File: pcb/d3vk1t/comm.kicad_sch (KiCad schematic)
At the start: 14 parts, among them IC5 TJA1042T/3/1J, IC6 MAX3485CSA+T, J4 Conn_01x03, J5 Conn_01x03

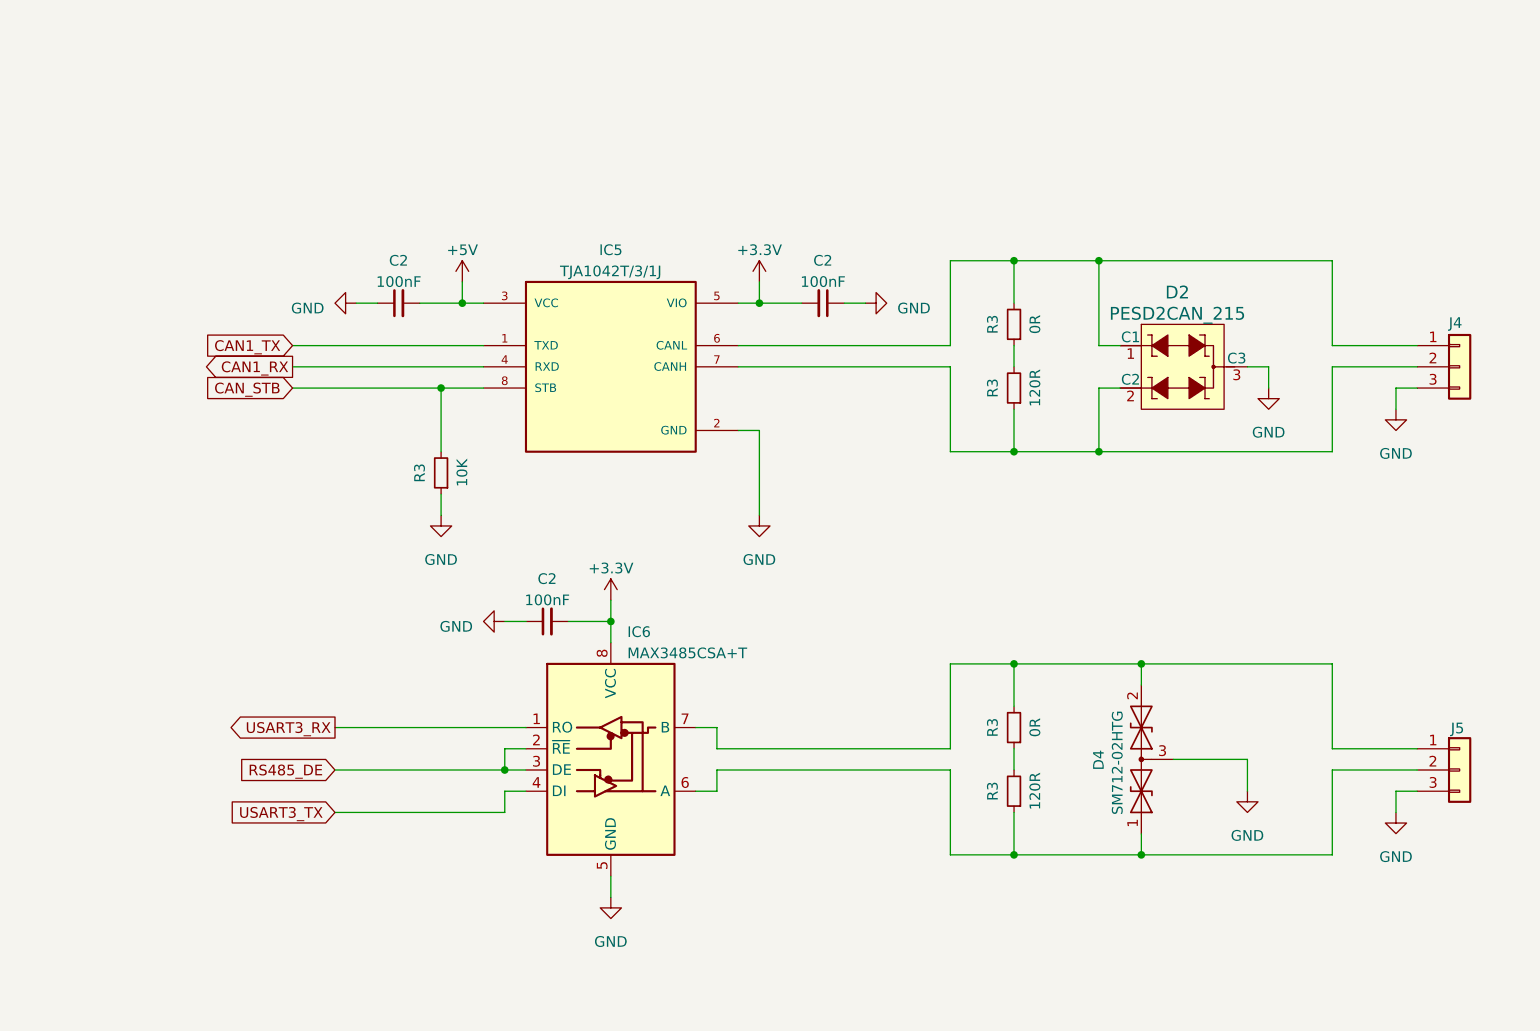
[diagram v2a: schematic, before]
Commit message: pcb: update layout
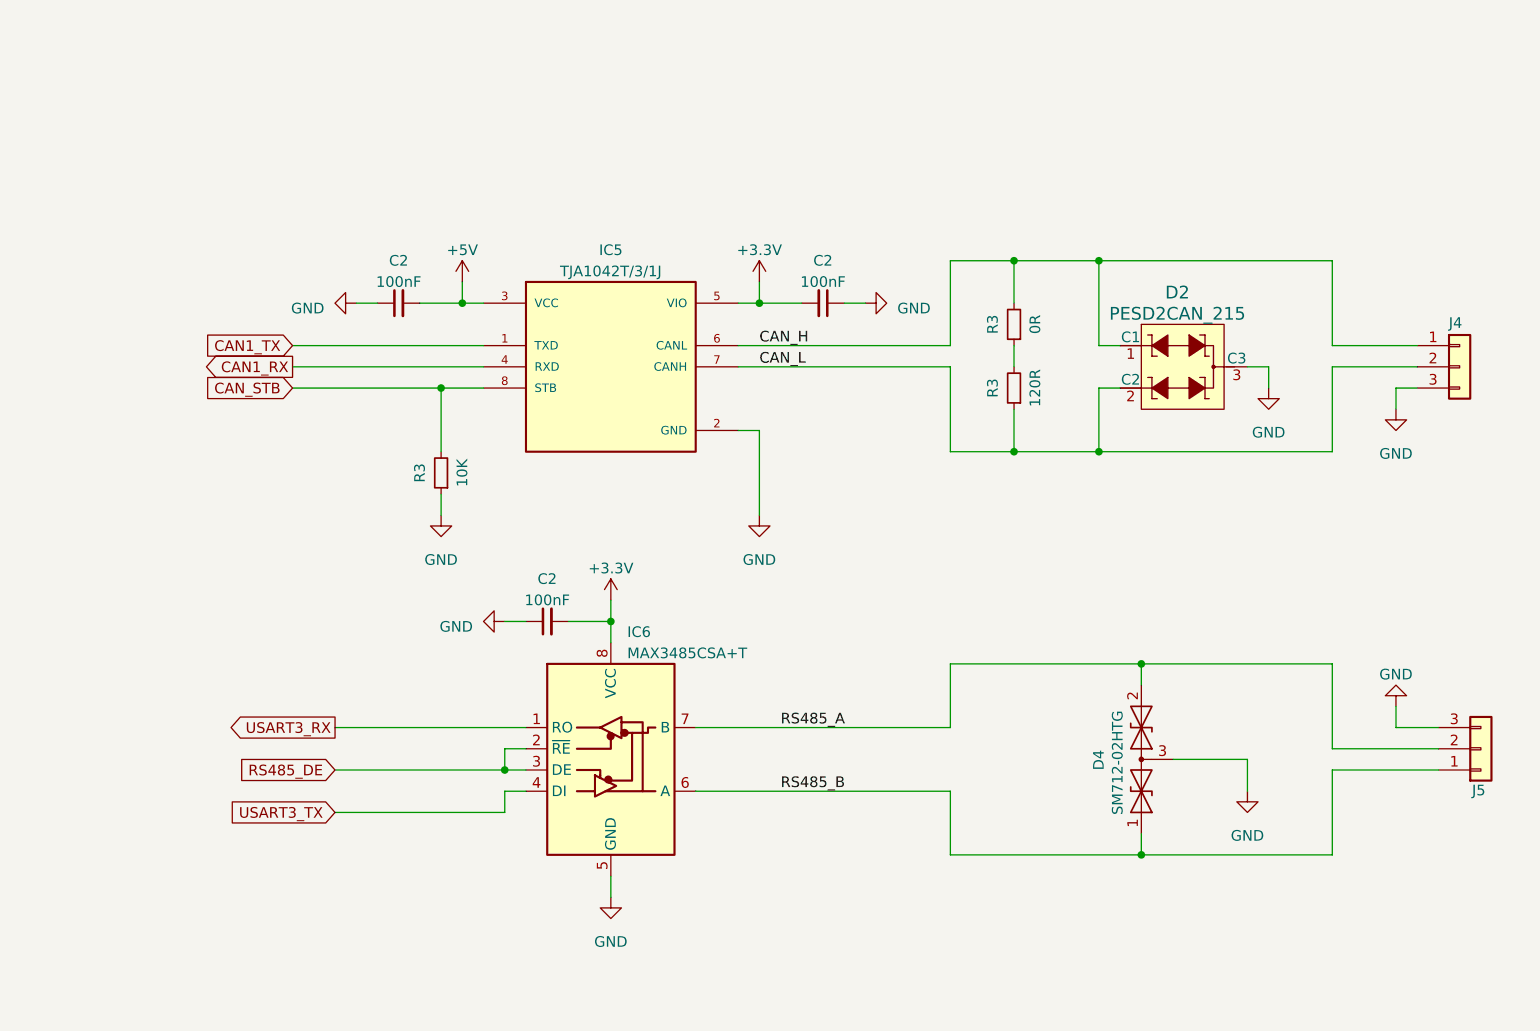
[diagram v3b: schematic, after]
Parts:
- removed R3: 120R, Resistor_SMD:R_0402_1005Metric, symbol Device:R_Small
- removed R3: 0R, Resistor_SMD:R_0402_1005Metric, symbol Device:R_Small
- D2: footprint digikey-footprints:SOT-23-3 -> bruno-libs:SOT-23B
- D4: footprint Package_TO_SOT_SMD:SOT-23 -> bruno-libs:SOT-23B
- IC6: footprint Package_SO:SOIC-8W_5.3x5.3mm_P1.27mm -> db:SOIC127P600X175-8N
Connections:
- net RS485_A: now reaches D4.2 (A2), IC6.7 (B)
- net RS485_A: now also J5.2 (Pin_2); no longer J5.1 (Pin_1)
- net RS485_B: now reaches D4.1 (A1), IC6.6 (A)
- net RS485_B: now also J5.1 (Pin_1); no longer J5.2 (Pin_2)
- net CAN_L: now reaches D2.2 (C2), IC5.7 (CANH), J4.2 (Pin_2), R3.1
- net CAN_H: now reaches D2.1 (C1), IC5.6 (CANL), J4.1 (Pin_1), R3.2
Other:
- moved on the sheet: J5
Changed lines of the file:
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@@
   (junction (at 187.96 86.36) (diameter 0) (color 0 0 0 0)
   )
-  (junction (at 177.8 134.62) (diameter 0) (color 0 0 0 0)
-  )
   (junction (at 187.96 63.5) (diameter 0) (color 0 0 0 0)
   )
   (junction (at 129.54 106.68) (diameter 0) (color 0 0 0 0)
   )
-  (junction (at 177.8 111.76) (diameter 0) (color 0 0 0 0)
-  )
   (junction (at 109.22 78.74) (diameter 0) (color 0 0 0 0)
   )
@@
     (stroke (width 0) (type default))
   )
-  (wire (pts (xy 215.9 121.92) (xy 226.06 121.92))
-    (stroke (width 0) (type default))
-  )
   (wire (pts (xy 109.22 86.36) (xy 109.22 78.74))
     (stroke (width 0) (type default))
@@
     (stroke (width 0) (type default))
   )
-  (wire (pts (xy 177.8 134.62) (xy 193.04 134.62))
-    (stroke (width 0) (type default))
-  )
   (wire (pts (xy 109.22 91.44) (xy 109.22 93.98))
     (stroke (width 0) (type default))
@@
     (stroke (width 0) (type default))
   )
-  (wire (pts (xy 170.18 111.76) (xy 177.8 111.76))
-    (stroke (width 0) (type default))
-  )
-  (wire (pts (xy 223.52 129.54) (xy 223.52 127))
+  (wire (pts (xy 223.52 119.38) (xy 223.52 116.84))
     (stroke (width 0) (type default))
   )
@@
     (stroke (width 0) (type default))
   )
-  (wire (pts (xy 177.8 121.92) (xy 177.8 124.46))
-    (stroke (width 0) (type default))
-  )
   (wire (pts (xy 124.46 106.68) (xy 129.54 106.68))
     (stroke (width 0) (type default))
@@
     (stroke (width 0) (type default))
   )
-  (wire (pts (xy 215.9 124.46) (xy 226.06 124.46))
-    (stroke (width 0) (type default))
-  )
-  (wire (pts (xy 170.18 124.46) (xy 170.18 134.62))
+  (wire (pts (xy 223.52 119.38) (xy 228.6 119.38))
+    (stroke (width 0) (type default))
+  )
+  (wire (pts (xy 170.18 127) (xy 170.18 134.62))
     (stroke (width 0) (type default))
   )
@@
     (stroke (width 0) (type default))
   )
-  (wire (pts (xy 177.8 111.76) (xy 193.04 111.76))
+  (wire (pts (xy 170.18 111.76) (xy 193.04 111.76))
     (stroke (width 0) (type default))
   )
@@
     (stroke (width 0) (type default))
   )
+  (wire (pts (xy 215.9 124.46) (xy 228.6 124.46))
+    (stroke (width 0) (type default))
+  )
   (wire (pts (xy 91.44 78.74) (xy 109.22 78.74))
     (stroke (width 0) (type default))
@@
     (stroke (width 0) (type default))
   )
-  (wire (pts (xy 139.7 127) (xy 142.24 127))
-    (stroke (width 0) (type default))
-  )
-  (wire (pts (xy 177.8 111.76) (xy 177.8 116.84))
+  (wire (pts (xy 139.7 127) (xy 170.18 127))
     (stroke (width 0) (type default))
   )
@@
     (stroke (width 0) (type default))
   )
-  (wire (pts (xy 170.18 134.62) (xy 177.8 134.62))
-    (stroke (width 0) (type default))
-  )
-  (wire (pts (xy 139.7 119.38) (xy 142.24 119.38))
-    (stroke (width 0) (type default))
-  )
-  (wire (pts (xy 142.24 121.92) (xy 142.24 119.38))
+  (wire (pts (xy 170.18 134.62) (xy 193.04 134.62))
     (stroke (width 0) (type default))
   )
@@
     (stroke (width 0) (type default))
   )
-  (wire (pts (xy 142.24 124.46) (xy 170.18 124.46))
-    (stroke (width 0) (type default))
-  )
   (wire (pts (xy 215.9 86.36) (xy 215.9 76.2))
     (stroke (width 0) (type default))
   )
-  (wire (pts (xy 142.24 121.92) (xy 170.18 121.92))
-    (stroke (width 0) (type default))
-  )
-  (wire (pts (xy 223.52 127) (xy 226.06 127))
+  (wire (pts (xy 139.7 119.38) (xy 170.18 119.38))
     (stroke (width 0) (type default))
   )
@@
     (stroke (width 0) (type default))
   )
-  (wire (pts (xy 170.18 121.92) (xy 170.18 111.76))
-    (stroke (width 0) (type default))
-  )
-  (wire (pts (xy 142.24 127) (xy 142.24 124.46))
+  (wire (pts (xy 170.18 119.38) (xy 170.18 111.76))
     (stroke (width 0) (type default))
   )
@@
     (stroke (width 0) (type default))
   )
+  (wire (pts (xy 215.9 121.92) (xy 228.6 121.92))
+    (stroke (width 0) (type default))
+  )
   (wire (pts (xy 116.84 124.46) (xy 119.38 124.46))
     (stroke (width 0) (type default))
@@
     (stroke (width 0) (type default))
   )
-  (wire (pts (xy 177.8 129.54) (xy 177.8 134.62))
-    (stroke (width 0) (type default))
+  (label "CAN_H" (at 147.32 73.66 0) (fields_autoplaced)
+    (effects (font (size 1.27 1.27)) (justify left bottom))
+  )
+  (label "RS485_A" (at 149.86 119.38 0) (fields_autoplaced)
+    (effects (font (size 1.27 1.27)) (justify left bottom))
+  )
+  (label "RS485_B" (at 149.86 127 0) (fields_autoplaced)
+    (effects (font (size 1.27 1.27)) (justify left bottom))
+  )
+  (label "CAN_L" (at 147.32 76.2 0) (fields_autoplaced)
+    (effects (font (size 1.27 1.27)) (justify left bottom))
   )
   (global_label "CAN1_TX" (shape input) (at 91.44 73.66 180) (fields_autoplaced)
@@
     )
   )
-  (symbol (lib_id "Connector_Generic:Conn_01x03") (at 231.14 124.46 0) (unit 1)
+  (symbol (lib_id "Connector_Generic:Conn_01x03") (at 233.68 121.92 0) (mirror x) (unit 1)
     (in_bom yes) (on_board yes) (dnp no)
-    (property "Reference" "J5" (at 230.0818 119.4761 0)
+    (property "Reference" "J5" (at 232.6218 126.9039 0)
       (effects (font (size 1.27 1.27)) (justify left))
     )
-    (property "Value" "Conn_01x03" (at 233.68 126.365 0)
+    (property "Value" "Conn_01x03" (at 236.22 120.015 0)
       (effects (font (size 1.27 1.27)) (justify left) hide)
     )
-    (property "Footprint" "Connector_JST:JST_XH_B3B-XH-A_1x03_P2.50mm_Vertical" (at 231.14 124.46 0)
-      (effects (font (size 1.27 1.27)) hide)
-    )
-    (property "Datasheet" "~" (at 231.14 124.46 0)
+    (property "Footprint" "Connector_JST:JST_XH_B3B-XH-A_1x03_P2.50mm_Vertical" (at 233.68 121.92 0)
+      (effects (font (size 1.27 1.27)) hide)
+    )
+    (property "Datasheet" "~" (at 233.68 121.92 0)
       (effects (font (size 1.27 1.27)) hide)
     )
@@
     )
   )
-  (symbol (lib_id "Device:R_Small") (at 177.8 127 180) (unit 1)
-    (in_bom yes) (on_board yes) (dnp no)
-    (property "Reference" "R3" (at 175.26 127 90)
-      (effects (font (size 1.27 1.27)))
-    )
-    (property "Value" "120R" (at 180.34 127 90)
-      (effects (font (size 1.27 1.27)))
-    )
-    (property "Footprint" "Resistor_SMD:R_0402_1005Metric" (at 177.8 127 0)
-      (effects (font (size 1.27 1.27)) hide)
-    )
-    (property "Datasheet" "~" (at 177.8 127 0)
-      (effects (font (size 1.27 1.27)) hide)
-    )
-    (pin "1")
-    (pin "2")
-    (instances
-      (project "d3vk1t"
-        (path "/4ea523ae-7c45-478e-a9cc-6f4833d1a9d5/41f8e312-86c0-4917-8944-524577576fad"
-          (reference "R3") (unit 1)
-        )
-        (path "/4ea523ae-7c45-478e-a9cc-6f4833d1a9d5/ee5fa9de-078f-4c07-8a01-b202c218757d"
-          (reference "R24") (unit 1)
-        )
-      )
-    )
-  )
-  (symbol (lib_id "power:GND") (at 223.52 129.54 0) (unit 1)
-    (in_bom yes) (on_board yes) (dnp no) (fields_autoplaced)
-    (property "Reference" "#PWR07" (at 223.52 135.89 0)
-      (effects (font (size 1.27 1.27)) hide)
-    )
-    (property "Value" "GND" (at 223.52 134.874 0)
-      (effects (font (size 1.27 1.27)))
-    )
-    (property "Footprint" "" (at 223.52 129.54 0)
-      (effects (font (size 1.27 1.27)) hide)
-    )
-    (property "Datasheet" "" (at 223.52 129.54 0)
+  (symbol (lib_id "power:GND") (at 223.52 116.84 180) (unit 1)
+    (in_bom yes) (on_board yes) (dnp no) (fields_autoplaced)
+    (property "Reference" "#PWR07" (at 223.52 110.49 0)
+      (effects (font (size 1.27 1.27)) hide)
+    )
+    (property "Value" "GND" (at 223.52 113.03 0)
+      (effects (font (size 1.27 1.27)))
+    )
+    (property "Footprint" "" (at 223.52 116.84 0)
+      (effects (font (size 1.27 1.27)) hide)
+    )
+    (property "Datasheet" "" (at 223.52 116.84 0)
       (effects (font (size 1.27 1.27)) hide)
     )
@@
       (effects (font (size 1.524 1.524)))
     )
-    (property "Footprint" "digikey-footprints:SOT-23-3" (at 203.2 71.12 0)
+    (property "Footprint" "bruno-libs:SOT-23B" (at 203.2 71.12 0)
       (effects (font (size 1.524 1.524)) (justify left) hide)
     )
@@
       (effects (font (size 1.27 1.27)) (justify left))
     )
-    (property "Footprint" "Package_SO:SOIC-8W_5.3x5.3mm_P1.27mm" (at 129.54 139.7 0)
+    (property "Footprint" "db:SOIC127P600X175-8N" (at 129.54 139.7 0)
       (effects (font (size 1.27 1.27)) hide)
     )
@@
     )
   )
-  (symbol (lib_id "Device:R_Small") (at 177.8 119.38 180) (unit 1)
-    (in_bom yes) (on_board yes) (dnp no)
-    (property "Reference" "R3" (at 175.26 119.38 90)
-      (effects (font (size 1.27 1.27)))
-    )
-    (property "Value" "0R" (at 180.34 119.38 90)
-      (effects (font (size 1.27 1.27)))
-    )
-    (property "Footprint" "Resistor_SMD:R_0402_1005Metric" (at 177.8 119.38 0)
-      (effects (font (size 1.27 1.27)) hide)
-    )
-    (property "Datasheet" "~" (at 177.8 119.38 0)
-      (effects (font (size 1.27 1.27)) hide)
-    )
-    (pin "1")
-    (pin "2")
-    (instances
-      (project "d3vk1t"
-        (path "/4ea523ae-7c45-478e-a9cc-6f4833d1a9d5/41f8e312-86c0-4917-8944-524577576fad"
-          (reference "R3") (unit 1)
-        )
-        (path "/4ea523ae-7c45-478e-a9cc-6f4833d1a9d5/ee5fa9de-078f-4c07-8a01-b202c218757d"
-          (reference "R23") (unit 1)
-        )
-      )
-    )
-  )
   (symbol (lib_id "db-can:TJA1042T,118") (at 129.54 73.66 0) (unit 1)
     (in_bom yes) (on_board yes) (dnp no) (fields_autoplaced)
@@
       (effects (font (size 1.27 1.27)) (justify left))
     )
-    (property "Footprint" "Package_TO_SOT_SMD:SOT-23" (at 201.93 123.19 0)
-      (effects (font (size 1.27 1.27)) hide)
-    )
+    (property "Footprint" "bruno-libs:SOT-23B" (at 201.93 123.19 0)
+      (effects (font (size 1.27 1.27)) hide)
+    )

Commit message: project update  - update pcb layout.  - update schmatics sheets.  - added manufacturing files.  - added documentation files.
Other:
- note added: "CAN INTERFACE"
- note added: "RS485 INTERFACE"
- title: (none) -> Serial Communication
- moved on the sheet: C2, D2, D4, IC5, IC6, J4, J5, R3
